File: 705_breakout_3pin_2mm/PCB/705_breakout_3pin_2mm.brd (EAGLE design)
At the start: 15.2 x 24.1 mm, 4 parts

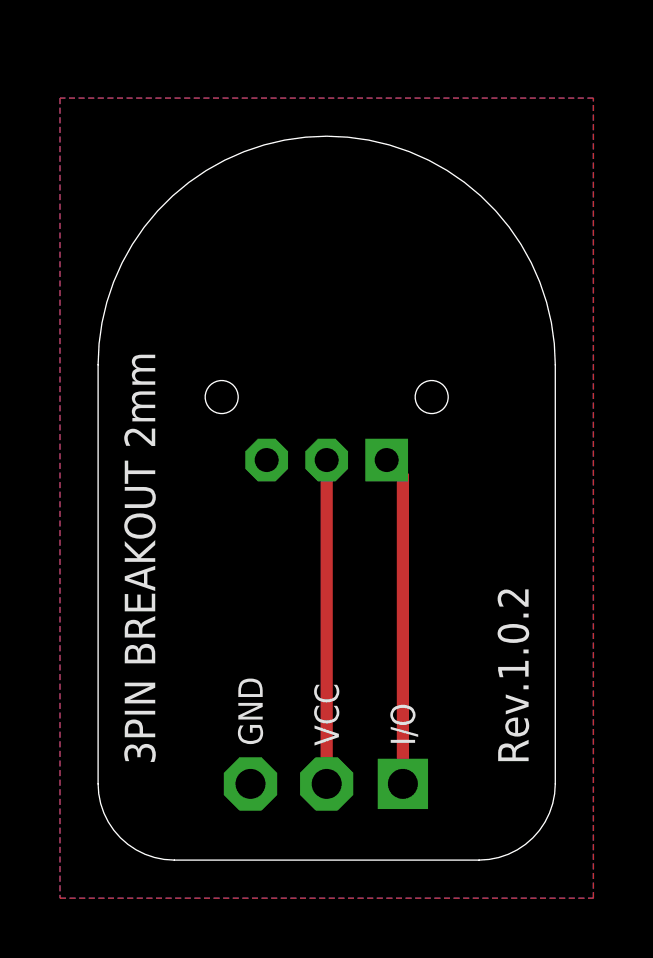
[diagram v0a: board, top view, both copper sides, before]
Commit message: fix solder land size
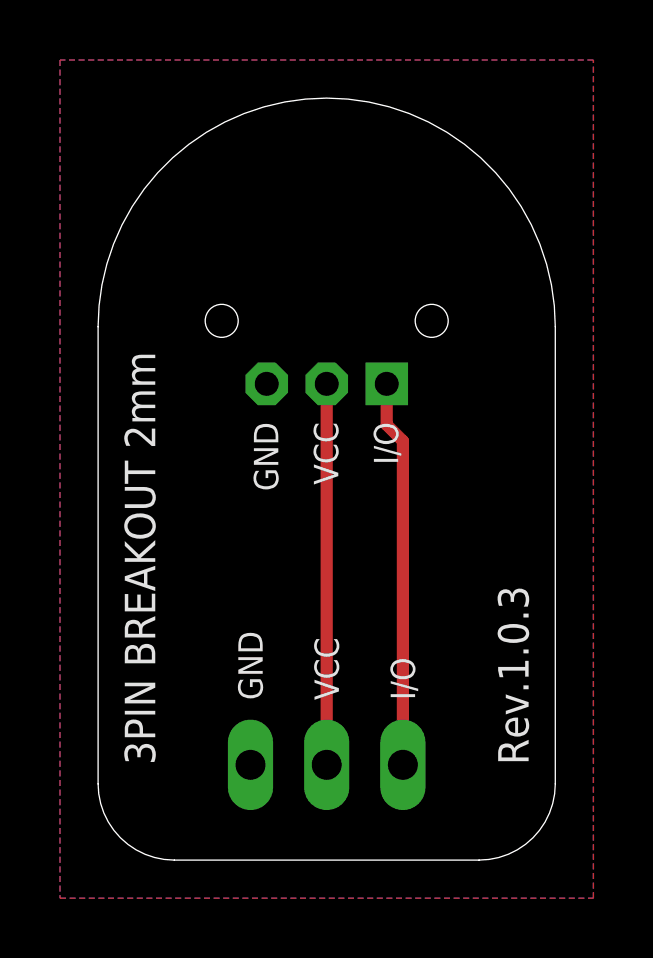
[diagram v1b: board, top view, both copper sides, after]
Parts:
- moved J2 2.54 mm to (7.62, 15.9)
- moved U$2 1.90 mm to (7.62, 19.7)
- moved J1 1.27 mm to (7.62, 14.0)
- moved U$3 0.63 mm to (7.62, 6.35)
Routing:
- net IO: track 11.0 -> 12.9 mm
- net VCC: track 10.8 -> 12.7 mm
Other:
- board size 15.2 x 24.1 mm -> 15.2 x 25.4 mm
- board text added: "GND"
- board text added: "I/O"
- board text added: "Rev.1.0.3"
- board text added: "VCC"
- board text removed: "Rev.1.0.2"
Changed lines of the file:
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@@
 <?xml version="1.0" encoding="utf-8"?>
 <!DOCTYPE eagle SYSTEM "eagle.dtd">
-<eagle version="7.4.0">
+<eagle version="7.5.0">
 <drawing>
 <settings>
@@
 <plain>
 <text x="1.905" y="3.175" size="1.016" layer="21" font="vector" ratio="12" rot="R90">3PIN BREAKOUT 2mm</text>
-<text x="13.335" y="3.175" size="1.016" layer="21" font="vector" ratio="12" rot="R90" align="top-left">Rev.1.0.2</text>
-<text x="7.62" y="17.78" size="0.8128" layer="22" font="vector" ratio="12" rot="MR180" align="bottom-center">MADE IN JAPAN</text>
-<text x="7.62" y="8.255" size="2.54" layer="22" font="vector" ratio="12" rot="MR0" align="bottom-center">#705</text>
+<text x="13.335" y="3.175" size="1.016" layer="21" font="vector" ratio="12" rot="R90" align="top-left">Rev.1.0.3</text>
+<text x="7.62" y="19.685" size="0.8128" layer="22" font="vector" ratio="12" rot="MR180" align="bottom-center">MADE IN JAPAN</text>
+<text x="7.62" y="10.16" size="2.54" layer="22" font="vector" ratio="12" rot="MR0" align="bottom-center">#705</text>
 <dimension x1="0" y1="-1.905" x2="15.24" y2="-1.905" x3="7.62" y3="-4.445" textsize="1.27" layer="51" visible="yes"/>
-<dimension x1="17.145" y1="0" x2="17.145" y2="24.13" x3="20.955003125" y3="12.065" textsize="1.27" layer="51" visible="yes"/>
+<dimension x1="17.145" y1="0" x2="17.145" y2="25.4" x3="20.955003125" y3="12.7" textsize="1.27" layer="51" visible="yes"/>
+<text x="9.6" y="14.6" size="0.8128" layer="21" font="vector" ratio="12" rot="R270" align="center-left">I/O</text>
+<text x="7.6" y="14.6" size="0.8128" layer="21" font="vector" ratio="12" rot="R270" align="center-left">VCC</text>
+<text x="5.6" y="14.6" size="0.8128" layer="21" font="vector" ratio="12" rot="R270" align="center-left">GND</text>
 </plain>
 <attributes>
@@
 </autorouter>
 <elements>
-<element name="J1" library="FaBo-Template" package="FABO_BRICK_3PIN_BREAKOUT" value="" x="7.62" y="12.7" smashed="yes"/>
-<element name="U$2" library="FaBo-etc" package="LOGO_FABO_MS_BOTTOM" value="" x="7.62" y="17.78"/>
-<element name="U$3" library="FaBo-etc" package="LOGO_OSHW_S_BOTTOM" value="" x="7.62" y="5.715"/>
-<element name="J2" library="FaBo-Template" package="FABO_BRICK_3PIN_S03B-PASK-2" value="" x="7.62" y="13.335" smashed="yes"/>
+<element name="J1" library="FaBo-Template" package="FABO_BRICK_3PIN_BREAKOUT" value="" x="7.62" y="13.97" smashed="yes"/>
+<element name="U$2" library="FaBo-etc" package="LOGO_FABO_MS_BOTTOM" value="" x="7.62" y="19.685"/>
+<element name="U$3" library="FaBo-etc" package="LOGO_OSHW_S_BOTTOM" value="" x="7.62" y="6.35"/>
+<element name="J2" library="FaBo-Template" package="FABO_BRICK_3PIN_S03B-PASK-2" value="" x="7.62" y="15.875" smashed="yes"/>
 </elements>
 <signals>
 <signal name="GND">
 <contactref element="J1" pad="GND"/>
-<polygon width="0.3048" layer="16" spacing="0.254">
+<contactref element="J2" pad="GND"/>
+<polygon width="0.2032" layer="16" spacing="0.254">
 <vertex x="-1.27" y="-1.27"/>
 <vertex x="16.51" y="-1.27"/>
-<vertex x="16.51" y="25.4"/>
-<vertex x="-1.27" y="25.4"/>
+<vertex x="16.51" y="26.67"/>
+<vertex x="-1.27" y="26.67"/>
 </polygon>
-<polygon width="0.3048" layer="1" spacing="0.254">
+<polygon width="0.2032" layer="1" spacing="0.254">
 <vertex x="-1.27" y="-1.27"/>
 <vertex x="16.51" y="-1.27"/>
-<vertex x="16.51" y="25.4"/>
-<vertex x="-1.27" y="25.4"/>
+<vertex x="16.51" y="26.67"/>
+<vertex x="-1.27" y="26.67"/>
 </polygon>
-<contactref element="J2" pad="GND"/>
 </signal>
 <signal name="VCC">
 <contactref element="J1" pad="VCC"/>
 <contactref element="J2" pad="VCC"/>
-<wire x1="7.62" y1="13.335" x2="7.62" y2="2.54" width="0.4064" layer="1"/>
+<wire x1="7.62" y1="15.875" x2="7.62" y2="3.175" width="0.4064" layer="1"/>
 </signal>
 <signal name="IO">
 <contactref element="J1" pad="I/O"/>
 <contactref element="J2" pad="I/O"/>
-<wire x1="9.62" y1="13.335" x2="10.16" y2="12.795" width="0.4064" layer="1"/>
-<wire x1="10.16" y1="12.795" x2="10.16" y2="2.54" width="0.4064" layer="1"/>
+<wire x1="9.62" y1="15.875" x2="9.62" y2="14.51" width="0.4064" layer="1"/>
+<wire x1="9.62" y1="14.51" x2="10.16" y2="13.97" width="0.4064" layer="1"/>
+<wire x1="10.16" y1="13.97" x2="10.16" y2="3.175" width="0.4064" layer="1"/>
 </signal>
 </signals>
